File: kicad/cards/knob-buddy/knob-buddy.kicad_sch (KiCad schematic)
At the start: 18 parts, among them J1 Conn_01x06_Pin, J2 Conn_01x06_Pin, J4 Conn_01x05, U1 THVD1450DR, U2 STM32C011F4Px

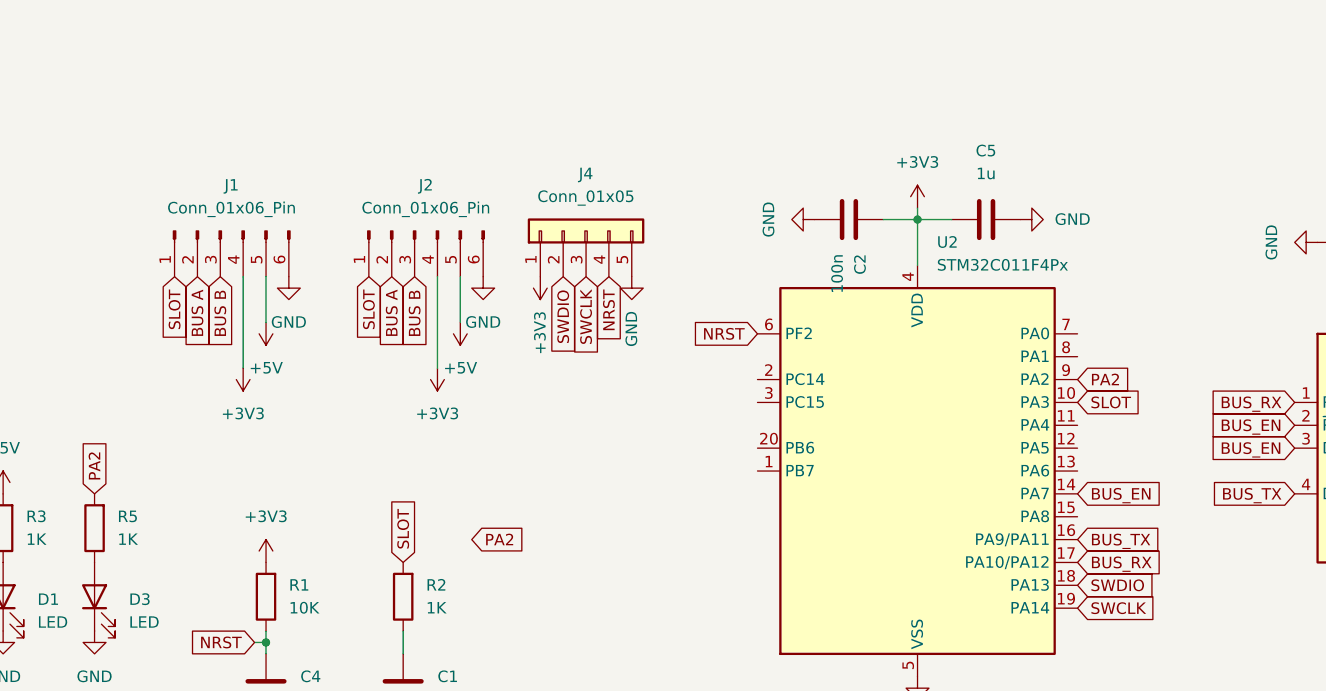
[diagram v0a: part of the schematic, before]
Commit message: Add card template and knob card
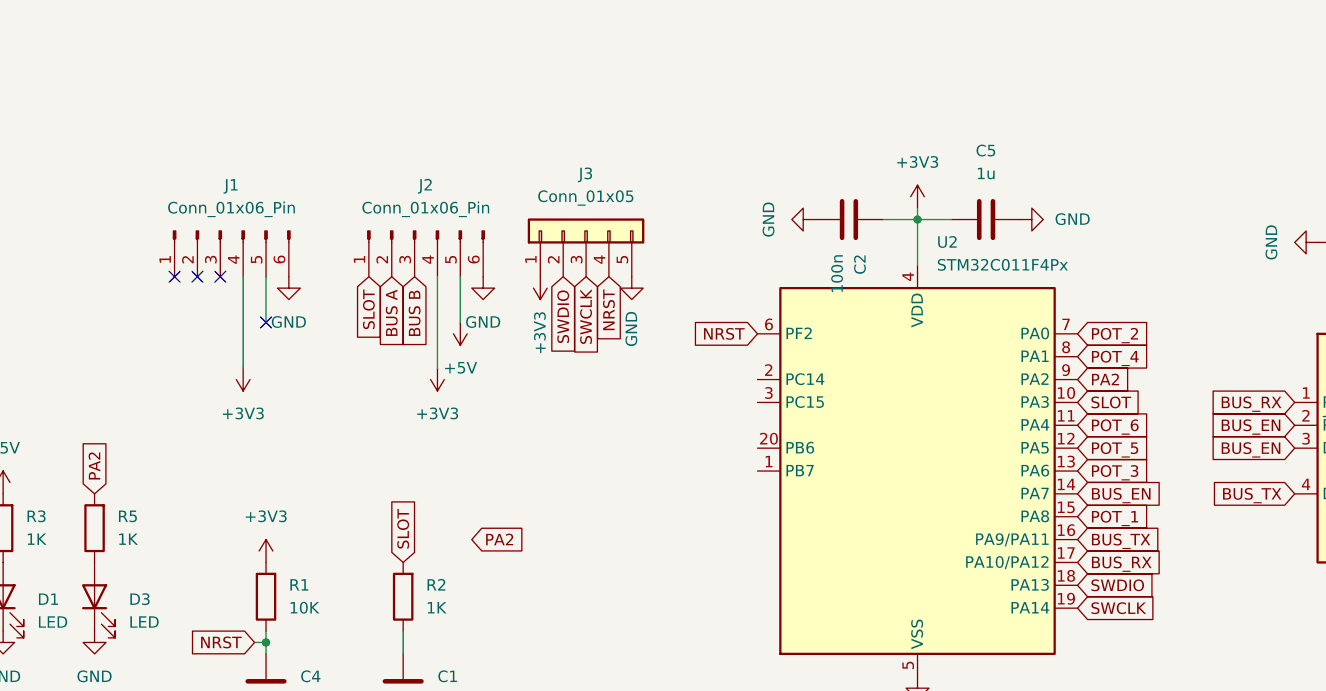
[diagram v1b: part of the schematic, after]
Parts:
- renumbered J4 to J3
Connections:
- net +5V: no longer J1.5 (Pin_5)
- net BUS A: no longer J1.2 (Pin_2)
- net BUS B: no longer J1.3 (Pin_3)
- net SLOT: no longer J1.1 (Pin_1)
- net POT_6: now reaches U2.11 (PA4)
- net POT_5: now reaches U2.12 (PA5)
- net POT_3: now reaches U2.13 (PA6)
- net POT_1: now reaches U2.15 (PA8)
- net POT_2: now reaches U2.7 (PA0)
- net POT_4: now reaches U2.8 (PA1)
- no-connect marks 0 -> 4
